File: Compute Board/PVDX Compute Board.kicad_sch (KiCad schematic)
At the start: 0 parts

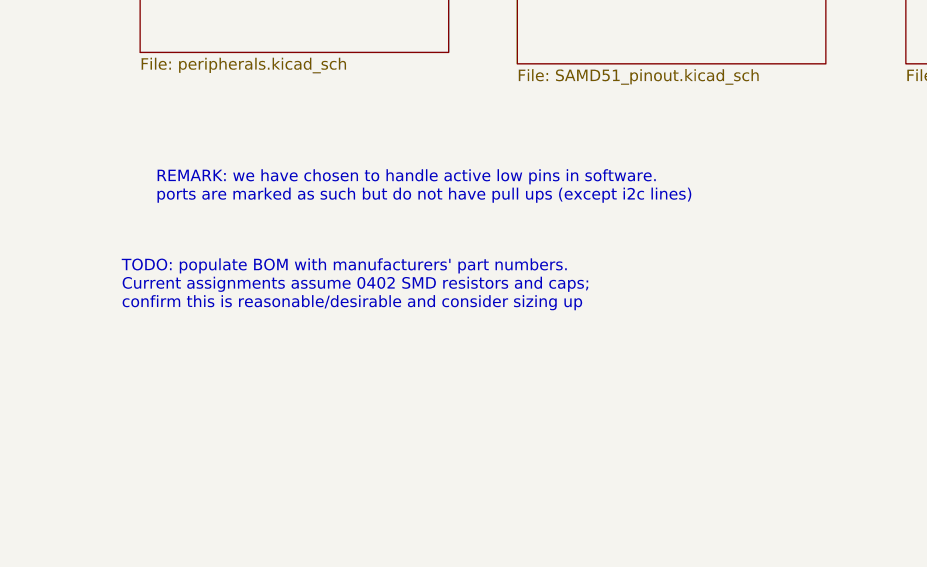
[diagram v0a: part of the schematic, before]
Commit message: Push layout-ready schematics and partial routing
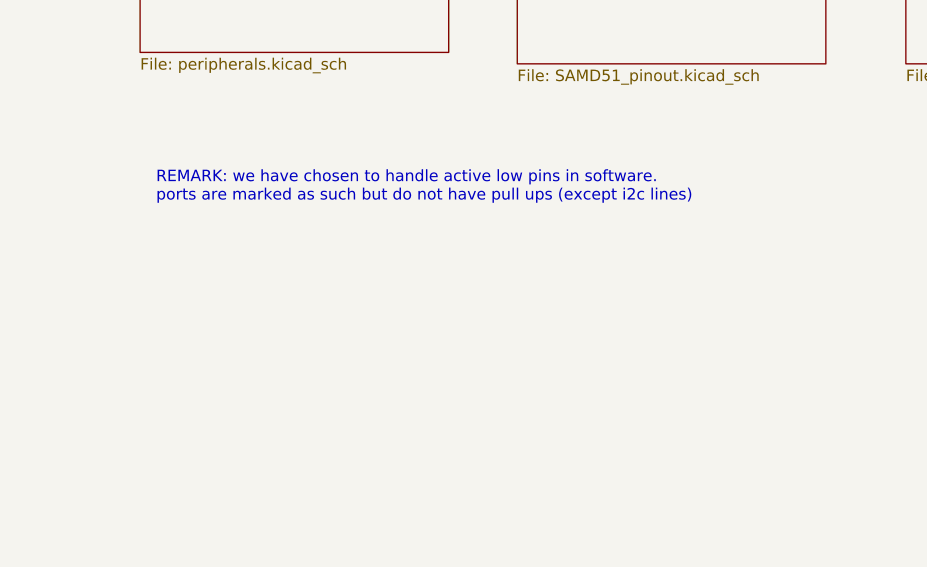
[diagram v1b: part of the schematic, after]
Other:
- note removed: "TODO: populate BOM with manufacturers' part numbers. Current assignments assume 0402 SMD resistors and caps; confirm this is reasonable/desirable and consider sizing up"
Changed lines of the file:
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@@
 	(generator_version "10.0")
 	(paper "A4")
-	(text "TODO: populate BOM with manufacturers' part numbers. \nCurrent assignments assume 0402 SMD resistors and caps;\nconfirm this is reasonable/desirable and consider sizing up"
-		(exclude_from_sim no)
-		(at 41.148 72.898 0)
-		(effects
-			(font
-				(size 1.27 1.27)
-				(color 255 0 0 1)
-			)
-			(justify left)
-		)
-	)
 	(text "REMARK: we have chosen to handle active low pins in software. \nports are marked as such but do not have pull ups (except i2c lines)"
 		(exclude_from_sim no)
